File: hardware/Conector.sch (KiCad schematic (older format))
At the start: 1 part

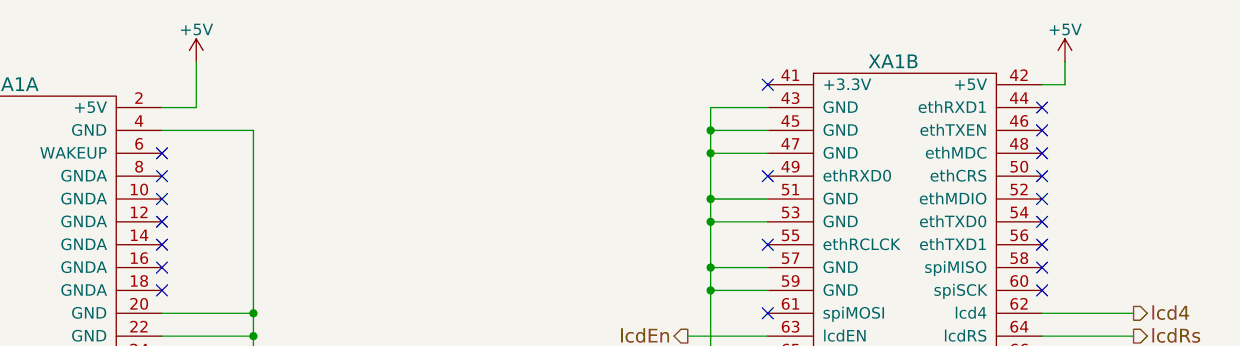
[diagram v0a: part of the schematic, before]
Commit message: Se finalizo esquematico del cricuito.
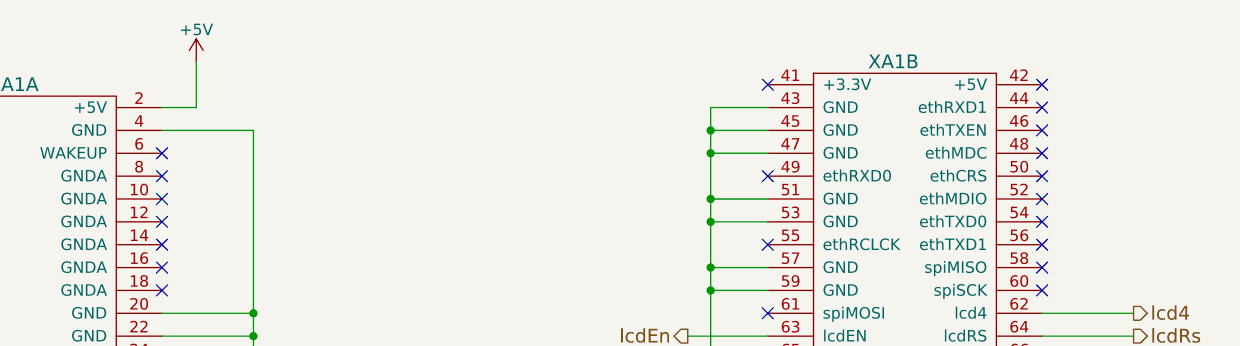
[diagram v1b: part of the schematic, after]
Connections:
- net +5V: no longer XA1.42 (+5V)
- no-connect marks 48 -> 49
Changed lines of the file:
@@
 encoding utf-8
 Sheet 5 5
-Title ""
-Date ""
+Title "Diagrama de conectores, para acoplar con la EDU-CIAA."
+Date "2016-07-04"
 Rev ""
-Comp ""
+Comp "Felipe Rey"
 Comment1 ""
 Comment2 ""
@@
 $EndComp
 $Comp
-L GND #PWR?
+L GND #PWR020
 U 1 1 5785D5F4
 P 5250 4400
-F 0 "#PWR?" H 5250 4150 50  0001 C CNN
+F 0 "#PWR020" H 5250 4150 50  0001 C CNN
 F 1 "GND" H 5250 4250 50  0000 C CNN
 F 2 "" H 5250 4400 60  0000 C CNN
@@
 $EndComp
 $Comp
-L +5V #PWR?
+L +5V #PWR021
 U 1 1 5785D61E
 P 5000 2150
-F 0 "#PWR?" H 5000 2000 50  0001 C CNN
+F 0 "#PWR021" H 5000 2000 50  0001 C CNN
 F 1 "+5V" H 5000 2290 50  0000 C CNN
 F 2 "" H 5000 2150 60  0000 C CNN
@@
 alert
 $Comp
-L GND #PWR?
+L GND #PWR022
 U 1 1 5785DC81
 P 7250 4450
-F 0 "#PWR?" H 7250 4200 50  0001 C CNN
+F 0 "#PWR022" H 7250 4200 50  0001 C CNN
 F 1 "GND" H 7250 4300 50  0000 C CNN
 F 2 "" H 7250 4450 60  0000 C CNN
@@
 	1    0    0    -1
 $EndComp
-Wire Wire Line
-	4850 2350 5000 2350
-Wire Wire Line
-	5000 2350 5000 2150
-Wire Wire Line
-	4850 4250 5250 4250
-Wire Wire Line
-	5250 2450 5250 4400
-Wire Wire Line
-	4850 2450 5250 2450
-Connection ~ 5250 4250
-Wire Wire Line
-	4850 3250 5250 3250
-Connection ~ 5250 3250
-Wire Wire Line
-	4850 3350 5250 3350
-Connection ~ 5250 3350
-Wire Wire Line
-	4850 3450 5250 3450
-Connection ~ 5250 3450
-Wire Wire Line
-	4850 3550 5250 3550
-Connection ~ 5250 3550
-Wire Wire Line
-	4850 3650 5250 3650
-Connection ~ 5250 3650
-Wire Wire Line
-	4850 3750 5250 3750
-Connection ~ 5250 3750
-Wire Wire Line
-	4850 3850 5250 3850
-Connection ~ 5250 3850
-Wire Wire Line
-	4850 4150 5250 4150
-Connection ~ 5250 4150
-Wire Wire Line
-	3200 3250 3650 3250
-Wire Wire Line
-	3650 3350 3350 3350
-Wire Wire Line
-	3350 3350 3350 3400
-Wire Wire Line
-	3350 3400 3200 3400
-Wire Wire Line
-	7150 3350 7500 3350
-Wire Wire Line
-	8700 3250 9100 3250
-Wire Wire Line
-	9100 3350 8700 3350
-Wire Wire Line
-	8700 3450 9100 3450
-Wire Wire Line
-	9100 3550 8700 3550
-Wire Wire Line
-	8700 3650 9100 3650
-Wire Wire Line
-	9100 3750 8700 3750
-Wire Wire Line
-	7500 2350 7250 2350
-Wire Wire Line
-	7250 2350 7250 4450
-Wire Wire Line
-	7500 2450 7250 2450
-Connection ~ 7250 2450
-Wire Wire Line
-	7500 2550 7250 2550
-Connection ~ 7250 2550
-Wire Wire Line
-	7500 2750 7250 2750
-Connection ~ 7250 2750
-Wire Wire Line
-	7500 2850 7250 2850
-Connection ~ 7250 2850
-Wire Wire Line
-	7500 3050 7250 3050
-Connection ~ 7250 3050
-Wire Wire Line
-	7500 3150 7250 3150
-Connection ~ 7250 3150
-Wire Wire Line
-	7500 3450 7250 3450
-Connection ~ 7250 3450
-Wire Wire Line
-	7500 3550 7250 3550
-Connection ~ 7250 3550
-Wire Wire Line
-	7500 4050 7250 4050
-Connection ~ 7250 4050
-Wire Wire Line
-	7500 4150 7250 4150
-Connection ~ 7250 4150
 NoConn ~ 7500 3950
 NoConn ~ 7500 3850
@@
 NoConn ~ 8700 4050
 NoConn ~ 8700 4150
-$Comp
-L +5V #PWR?
-U 1 1 5785E114
-P 8800 2150
-F 0 "#PWR?" H 8800 2000 50  0001 C CNN
-F 1 "+5V" H 8800 2290 50  0000 C CNN
-F 2 "" H 8800 2150 60  0000 C CNN
-F 3 "" H 8800 2150 60  0000 C CNN
-	1    8800 2150
-	1    0    0    -1
-$EndComp
-Wire Wire Line
-	8800 2150 8800 2250
-Wire Wire Line
-	8800 2250 8700 2250
 NoConn ~ 3650 2350
+Wire Wire Line
+	4850 4250 5250 4250
+Wire Wire Line
+	5250 2450 5250 4400
+Wire Wire Line
+	4850 2450 5250 2450
+Connection ~ 5250 4250
+Wire Wire Line
+	4850 3250 5250 3250
+Connection ~ 5250 3250
+Wire Wire Line
+	4850 3350 5250 3350
+Connection ~ 5250 3350
+Wire Wire Line
+	4850 3450 5250 3450
+Connection ~ 5250 3450
+Wire Wire Line
+	4850 3550 5250 3550
+Connection ~ 5250 3550
+Wire Wire Line
+	4850 3650 5250 3650
+Connection ~ 5250 3650
+Wire Wire Line
+	4850 3750 5250 3750
+Connection ~ 5250 3750
+Wire Wire Line
+	4850 3850 5250 3850
+Connection ~ 5250 3850
+Wire Wire Line
+	4850 4150 5250 4150
+Connection ~ 5250 4150
+Wire Wire Line
+	3200 3250 3650 3250
+Wire Wire Line
+	3650 3350 3350 3350
+Wire Wire Line
+	3350 3350 3350 3400
+Wire Wire Line
+	3350 3400 3200 3400
+Wire Wire Line
+	7150 3350 7500 3350
+Wire Wire Line
+	8700 3250 9100 3250
+Wire Wire Line
+	9100 3350 8700 3350
+Wire Wire Line
+	8700 3450 9100 3450
+Wire Wire Line
+	9100 3550 8700 3550
+Wire Wire Line
+	8700 3650 9100 3650
+Wire Wire Line
+	9100 3750 8700 3750
+Wire Wire Line
+	7500 2350 7250 2350
+Wire Wire Line
+	7250 2350 7250 4450
+Wire Wire Line
+	7500 2450 7250 2450
+Connection ~ 7250 2450
+Wire Wire Line
+	7500 2550 7250 2550
+Connection ~ 7250 2550
+Wire Wire Line
+	7500 2750 7250 2750
+Connection ~ 7250 2750
+Wire Wire Line
+	7500 2850 7250 2850
+Connection ~ 7250 2850
+Wire Wire Line
+	7500 3050 7250 3050
+Connection ~ 7250 3050
+Wire Wire Line
+	7500 3150 7250 3150
+Connection ~ 7250 3150
+Wire Wire Line
+	7500 3450 7250 3450
+Connection ~ 7250 3450
+Wire Wire Line
+	7500 3550 7250 3550
+Connection ~ 7250 3550
+Wire Wire Line
+	7500 4050 7250 4050
+Connection ~ 7250 4050
+Wire Wire Line
+	7500 4150 7250 4150
+Connection ~ 7250 4150
+Wire Wire Line
+	5000 2150 5000 2350
+Wire Wire Line
+	5000 2350 4850 2350
+NoConn ~ 8700 2250
 $EndSCHEMATC

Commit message: Se cargaron los footprint de los componentes.
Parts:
- XA1: footprint (none) -> ej2cese:Conn_ponchoMediano
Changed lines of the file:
@@
 LIBS:valves
 LIBS:ej2cese
+LIBS:ADS1113IDGSR
 LIBS:poncho_celda-cache
 EELAYER 25 0
@@
 F 0 "XA1" H 4200 3050 60  0000 C CNN
 F 1 "Conn_Poncho2P_2x_20x2" H 4250 950 60  0000 C CNN
-F 2 "" H 3900 2650 60  0000 C CNN
+F 2 "ej2cese:Conn_ponchoMediano" H 3900 2650 60  0001 C CNN
 F 3 "" H 3900 2650 60  0000 C CNN
 	1    3900 2650
@@
 F 0 "XA1" H 8050 2950 60  0000 C CNN
 F 1 "Conn_Poncho2P_2x_20x2" H 8100 850 60  0000 C CNN
-F 2 "" H 7750 2550 60  0000 C CNN
+F 2 "ej2cese:Conn_ponchoMediano" H 7750 2550 60  0001 C CNN
 F 3 "" H 7750 2550 60  0000 C CNN
 	2    7750 2550

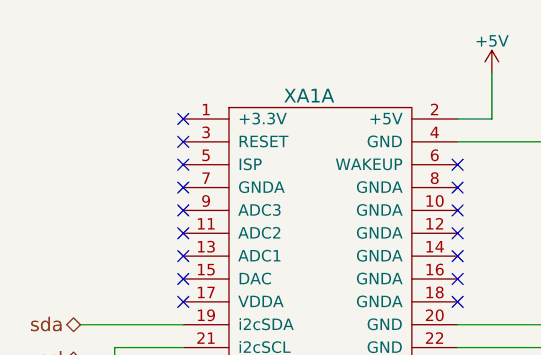
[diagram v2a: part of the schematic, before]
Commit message: Se realizo diseño de PCB doble capa.
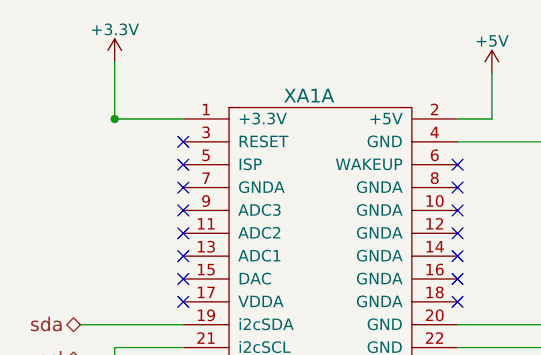
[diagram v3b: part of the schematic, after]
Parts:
- XA1: footprint ej2cese:Conn_ponchoMediano -> ej2cese:PonchoGrande
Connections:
- net +3V3: now reaches XA1.1 (+3.3V)
- no-connect marks 49 -> 48
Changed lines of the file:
@@
 F 0 "XA1" H 4200 3050 60  0000 C CNN
 F 1 "Conn_Poncho2P_2x_20x2" H 4250 950 60  0000 C CNN
-F 2 "ej2cese:Conn_ponchoMediano" H 3900 2650 60  0001 C CNN
+F 2 "ej2cese:PonchoGrande" H 3900 2650 60  0001 C CNN
 F 3 "" H 3900 2650 60  0000 C CNN
 	1    3900 2650
@@
 F 0 "XA1" H 8050 2950 60  0000 C CNN
 F 1 "Conn_Poncho2P_2x_20x2" H 8100 850 60  0000 C CNN
-F 2 "ej2cese:Conn_ponchoMediano" H 7750 2550 60  0001 C CNN
+F 2 "ej2cese:PonchoGrande" H 7750 2550 60  0001 C CNN
 F 3 "" H 7750 2550 60  0000 C CNN
 	2    7750 2550
@@
 NoConn ~ 7500 2950
 NoConn ~ 7500 2650
-NoConn ~ 7500 2250
 NoConn ~ 8700 2350
 NoConn ~ 8700 2450
@@
 NoConn ~ 8700 4050
 NoConn ~ 8700 4150
-NoConn ~ 3650 2350
 Wire Wire Line
 	4850 4250 5250 4250
@@
 	5000 2350 4850 2350
 NoConn ~ 8700 2250
+NoConn ~ 7500 2250
+Wire Wire Line
+	3350 2100 3350 2350
+Connection ~ 3350 2350
+Wire Wire Line
+	3350 2350 3650 2350
+$Comp
+L +3.3V #PWR023
+U 1 1 578EC122
+P 3350 2100
+F 0 "#PWR023" H 3350 1950 50  0001 C CNN
+F 1 "+3.3V" H 3350 2240 50  0000 C CNN
+F 2 "" H 3350 2100 50  0000 C CNN
+F 3 "" H 3350 2100 50  0000 C CNN
+	1    3350 2100
+	1    0    0    -1
+$EndComp
 $EndSCHEMATC

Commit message: Se realizan correcciones al esquematico.
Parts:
- XA1: footprint ej2cese:PonchoGrande -> celda:Conn_Poncho_SinBorde
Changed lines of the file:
@@
 $Descr A4 11693 8268
 encoding utf-8
-Sheet 5 5
+Sheet 5 3
 Title "Diagrama de conectores, para acoplar con la EDU-CIAA."
 Date "2016-07-04"
 Rev ""
 Comp "Felipe Rey"
-Comment1 ""
-Comment2 ""
+Comment1 "Diagrama esquematico de modulos para poncho celda para el curso de Diseño de PCB del CESE."
+Comment2 "Licencia GPL V3"
 Comment3 ""
 Comment4 ""
@@
 F 0 "XA1" H 4200 3050 60  0000 C CNN
 F 1 "Conn_Poncho2P_2x_20x2" H 4250 950 60  0000 C CNN
-F 2 "ej2cese:PonchoGrande" H 3900 2650 60  0001 C CNN
+F 2 "celda:Conn_Poncho_SinBorde" H 3900 2650 60  0001 C CNN
 F 3 "" H 3900 2650 60  0000 C CNN
 	1    3900 2650
@@
 F 0 "XA1" H 8050 2950 60  0000 C CNN
 F 1 "Conn_Poncho2P_2x_20x2" H 8100 850 60  0000 C CNN
-F 2 "ej2cese:PonchoGrande" H 7750 2550 60  0001 C CNN
+F 2 "celda:Conn_Poncho_SinBorde" H 7750 2550 60  0001 C CNN
 F 3 "" H 7750 2550 60  0000 C CNN
 	2    7750 2550
@@
 $EndComp
 $Comp
-L GND #PWR019
+L GND #PWR017
 U 1 1 5785D5F4
 P 5250 4400
-F 0 "#PWR019" H 5250 4150 50  0001 C CNN
+F 0 "#PWR017" H 5250 4150 50  0001 C CNN
 F 1 "GND" H 5250 4250 50  0000 C CNN
 F 2 "" H 5250 4400 60  0000 C CNN
@@
 $EndComp
 $Comp
-L +5V #PWR020
+L +5V #PWR018
 U 1 1 5785D61E
 P 5000 2150
-F 0 "#PWR020" H 5000 2000 50  0001 C CNN
+F 0 "#PWR018" H 5000 2000 50  0001 C CNN
 F 1 "+5V" H 5000 2290 50  0000 C CNN
 F 2 "" H 5000 2150 60  0000 C CNN
@@
 alert
 $Comp
-L GND #PWR021
+L GND #PWR019
 U 1 1 5785DC81
 P 7250 4450
-F 0 "#PWR021" H 7250 4200 50  0001 C CNN
+F 0 "#PWR019" H 7250 4200 50  0001 C CNN
 F 1 "GND" H 7250 4300 50  0000 C CNN
 F 2 "" H 7250 4450 60  0000 C CNN
@@
 	3350 2350 3650 2350
 $Comp
-L +3.3V #PWR022
+L +3.3V #PWR020
 U 1 1 578EC122
 P 3350 2100
-F 0 "#PWR022" H 3350 1950 50  0001 C CNN
+F 0 "#PWR020" H 3350 1950 50  0001 C CNN
 F 1 "+3.3V" H 3350 2240 50  0000 C CNN
 F 2 "" H 3350 2100 50  0000 C CNN
